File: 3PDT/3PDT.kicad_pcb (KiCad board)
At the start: 2 copper layers, 31.5 x 26.7 mm, 10 parts, among them J1 A1, J2 A2, J3 A3, J4 B1, J5 B2, J6 B3, J7 C1, J8 C2, J9 C3, sw1 3PDTFootswitch

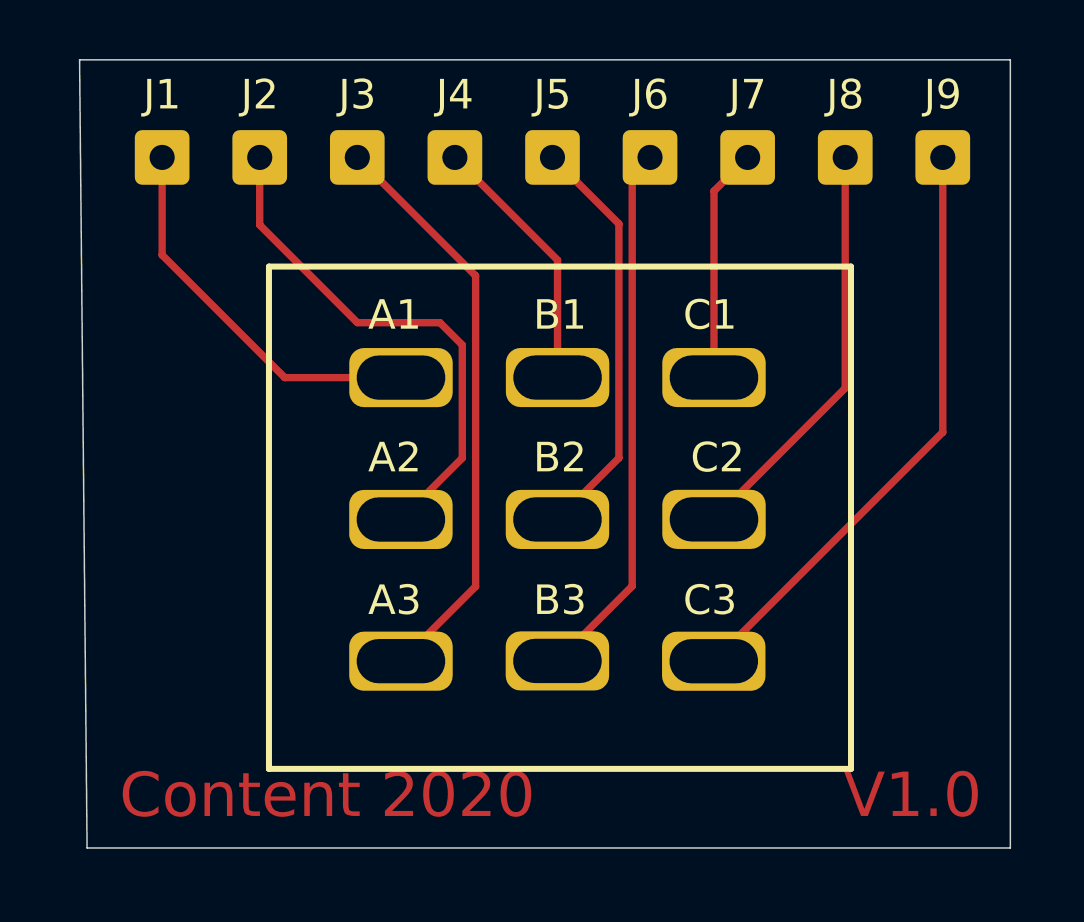
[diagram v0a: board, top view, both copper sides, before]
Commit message: Completed simple 3PDT board
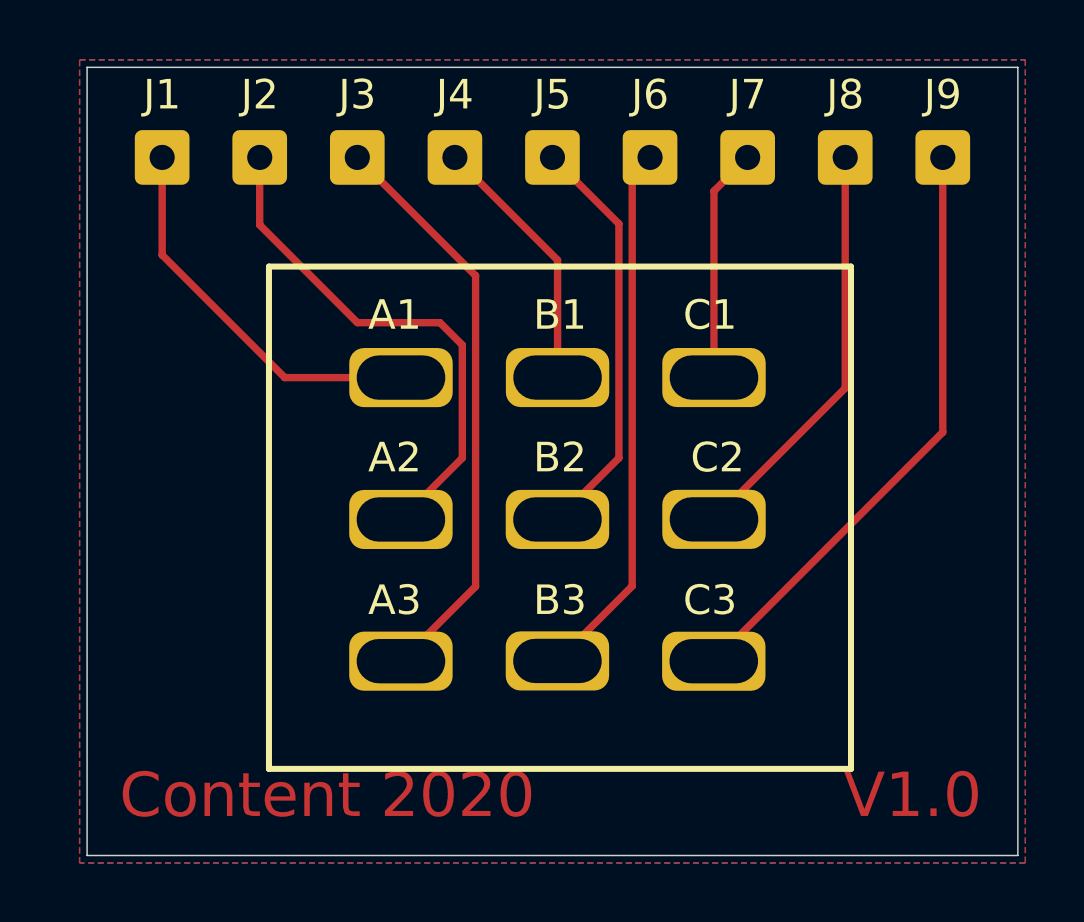
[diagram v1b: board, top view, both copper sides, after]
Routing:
- added copper zone on B.Cu, net (none)
- added copper zone on F.Cu, net (none)
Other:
- outline, holes or cut-outs redrawn
- rule pad_to_mask_clearance: 0.05 -> 0
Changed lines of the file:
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@@
-(kicad_pcb (version 20171130) (host pcbnew 5.1.6)
+(kicad_pcb (version 20171130) (host pcbnew 5.1.7)
   (general
     (thickness 1.6)
@@
     (pad_size 3.5 2)
     (pad_drill 3)
-    (pad_to_mask_clearance 0.05)
+    (pad_to_mask_clearance 0)
     (aux_axis_origin 0 0)
     (visible_elements FFFFFF7F)
@@
       (effects (font (size 0.42 0.42) (thickness 0.06)))
     )
-    (pad 1 thru_hole roundrect (at 0 0) (size 1.85 1.85) (drill 0.85) (layers *.Cu *.Mask) (roundrect_rratio 0.135135)
+    (pad 1 thru_hole roundrect (at 0 0) (size 1.85 1.85) (drill 0.85) (layers *.Cu *.Mask) (roundrect_rratio 0.1351345945945946)
       (net 1 "Net-(J1-Pad1)"))
     (model ${KISYS3DMOD}/Connector_Wire.3dshapes/SolderWire-0.25sqmm_1x01_D0.65mm_OD1.7mm.wrl
@@
       (effects (font (size 0.42 0.42) (thickness 0.06)))
     )
-    (pad 1 thru_hole roundrect (at 0 0) (size 1.85 1.85) (drill 0.85) (layers *.Cu *.Mask) (roundrect_rratio 0.135135)
+    (pad 1 thru_hole roundrect (at 0 0) (size 1.85 1.85) (drill 0.85) (layers *.Cu *.Mask) (roundrect_rratio 0.1351345945945946)
       (net 2 "Net-(J2-Pad1)"))
     (model ${KISYS3DMOD}/Connector_Wire.3dshapes/SolderWire-0.25sqmm_1x01_D0.65mm_OD1.7mm.wrl
@@
       (effects (font (size 0.42 0.42) (thickness 0.06)))
     )
-    (pad 1 thru_hole roundrect (at 0 0) (size 1.85 1.85) (drill 0.85) (layers *.Cu *.Mask) (roundrect_rratio 0.135135)
+    (pad 1 thru_hole roundrect (at 0 0) (size 1.85 1.85) (drill 0.85) (layers *.Cu *.Mask) (roundrect_rratio 0.1351345945945946)
       (net 3 "Net-(J3-Pad1)"))
     (model ${KISYS3DMOD}/Connector_Wire.3dshapes/SolderWire-0.25sqmm_1x01_D0.65mm_OD1.7mm.wrl
@@
       (effects (font (size 0.42 0.42) (thickness 0.06)))
     )
-    (pad 1 thru_hole roundrect (at 0 0) (size 1.85 1.85) (drill 0.85) (layers *.Cu *.Mask) (roundrect_rratio 0.135135)
+    (pad 1 thru_hole roundrect (at 0 0) (size 1.85 1.85) (drill 0.85) (layers *.Cu *.Mask) (roundrect_rratio 0.1351345945945946)
       (net 4 "Net-(J4-Pad1)"))
     (model ${KISYS3DMOD}/Connector_Wire.3dshapes/SolderWire-0.25sqmm_1x01_D0.65mm_OD1.7mm.wrl
@@
       (effects (font (size 0.42 0.42) (thickness 0.06)))
     )
-    (pad 1 thru_hole roundrect (at 0 0) (size 1.85 1.85) (drill 0.85) (layers *.Cu *.Mask) (roundrect_rratio 0.135135)
+    (pad 1 thru_hole roundrect (at 0 0) (size 1.85 1.85) (drill 0.85) (layers *.Cu *.Mask) (roundrect_rratio 0.1351345945945946)
       (net 5 "Net-(J5-Pad1)"))
     (model ${KISYS3DMOD}/Connector_Wire.3dshapes/SolderWire-0.25sqmm_1x01_D0.65mm_OD1.7mm.wrl
@@
       (effects (font (size 0.42 0.42) (thickness 0.06)))
     )
-    (pad 1 thru_hole roundrect (at 0 0) (size 1.85 1.85) (drill 0.85) (layers *.Cu *.Mask) (roundrect_rratio 0.135135)
+    (pad 1 thru_hole roundrect (at 0 0) (size 1.85 1.85) (drill 0.85) (layers *.Cu *.Mask) (roundrect_rratio 0.1351345945945946)
       (net 6 "Net-(J6-Pad1)"))
     (model ${KISYS3DMOD}/Connector_Wire.3dshapes/SolderWire-0.25sqmm_1x01_D0.65mm_OD1.7mm.wrl
@@
       (effects (font (size 0.42 0.42) (thickness 0.06)))
     )
-    (pad 1 thru_hole roundrect (at 0 0) (size 1.85 1.85) (drill 0.85) (layers *.Cu *.Mask) (roundrect_rratio 0.135135)
+    (pad 1 thru_hole roundrect (at 0 0) (size 1.85 1.85) (drill 0.85) (layers *.Cu *.Mask) (roundrect_rratio 0.1351345945945946)
       (net 7 "Net-(J7-Pad1)"))
     (model ${KISYS3DMOD}/Connector_Wire.3dshapes/SolderWire-0.25sqmm_1x01_D0.65mm_OD1.7mm.wrl
@@
       (effects (font (size 0.42 0.42) (thickness 0.06)))
     )
-    (pad 1 thru_hole roundrect (at 0 0) (size 1.85 1.85) (drill 0.85) (layers *.Cu *.Mask) (roundrect_rratio 0.135135)
+    (pad 1 thru_hole roundrect (at 0 0) (size 1.85 1.85) (drill 0.85) (layers *.Cu *.Mask) (roundrect_rratio 0.1351345945945946)
       (net 8 "Net-(J8-Pad1)"))
     (model ${KISYS3DMOD}/Connector_Wire.3dshapes/SolderWire-0.25sqmm_1x01_D0.65mm_OD1.7mm.wrl
@@
       (effects (font (size 0.42 0.42) (thickness 0.06)))
     )
-    (pad 1 thru_hole roundrect (at 0 0) (size 1.85 1.85) (drill 0.85) (layers *.Cu *.Mask) (roundrect_rratio 0.135135)
+    (pad 1 thru_hole roundrect (at 0 0) (size 1.85 1.85) (drill 0.85) (layers *.Cu *.Mask) (roundrect_rratio 0.1351345945945946)
       (net 9 "Net-(J9-Pad1)"))
     (model ${KISYS3DMOD}/Connector_Wire.3dshapes/SolderWire-0.25sqmm_1x01_D0.65mm_OD1.7mm.wrl
@@
       (net 7 "Net-(J7-Pad1)") (solder_mask_margin 0.1016))
   )
+  (gr_line (start 124.968 63.5) (end 156.464 63.5) (layer Edge.Cuts) (width 0.05))
+  (gr_line (start 124.968 90.17) (end 124.968 63.5) (layer Edge.Cuts) (width 0.05))
+  (gr_line (start 156.464 90.17) (end 124.968 90.17) (layer Edge.Cuts) (width 0.05))
+  (gr_line (start 156.464 63.5) (end 156.464 90.17) (layer Edge.Cuts) (width 0.05))
   (gr_text V1.0 (at 152.908 88.138) (layer F.Cu)
     (effects (font (size 1.5 1.5) (thickness 0.3)))
@@
     (effects (font (size 1 1) (thickness 0.15)))
   )
-  (gr_line (start 124.968 89.916) (end 124.714 63.246) (layer Edge.Cuts) (width 0.05))
-  (gr_line (start 156.21 89.916) (end 124.968 89.916) (layer Edge.Cuts) (width 0.05))
-  (gr_line (start 156.21 63.246) (end 156.21 89.916) (layer Edge.Cuts) (width 0.05))
-  (gr_line (start 124.714 63.246) (end 156.21 63.246) (layer Edge.Cuts) (width 0.05))
   (segment (start 135.59028 73.99842) (end 131.65642 73.99842) (width 0.25) (layer F.Cu) (net 1))
   (segment (start 127.508 69.85) (end 127.508 66.548) (width 0.25) (layer F.Cu) (net 1))
@@
   (segment (start 153.924 75.84694) (end 153.924 66.548) (width 0.25) (layer F.Cu) (net 9))
   (segment (start 146.17446 83.59648) (end 153.924 75.84694) (width 0.25) (layer F.Cu) (net 9))
+  (zone (net 0) (net_name "") (layer F.Cu) (hatch edge 0.508)
+    (connect_pads (clearance 0.508))
+    (min_thickness 0.254)
+    (fill yes (arc_segments 32) (thermal_gap 0.508) (thermal_bridge_width 0.508))
+    (polygon
+      (pts
+        (xy 156.718 90.424) (xy 124.714 90.424) (xy 124.714 63.246) (xy 156.718 63.246)
+      )
+    )
+  )
+  (zone (net 0) (net_name "") (layer B.Cu) (hatch edge 0.508)
+    (connect_pads (clearance 0.508))
+    (min_thickness 0.254)
+    (fill yes (arc_segments 32) (thermal_gap 0.508) (thermal_bridge_width 0.508))
+    (polygon
+      (pts
+        (xy 156.718 90.424) (xy 124.714 90.424) (xy 124.714 63.246) (xy 156.718 63.246)
+      )
+    )
+  )
 )
